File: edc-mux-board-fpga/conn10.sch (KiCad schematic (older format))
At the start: 24 parts

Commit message: Finished FPGA and MCU interconnections.
Finished up interrupt wiring
Fixed a few missing connections
Annotated Schematic
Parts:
- removed C? (x2): 1uF, Capacitor_SMD:C_0805_2012Metric, symbol Device:C_Small
- removed C? (x2): 2.2uF X7R, Capacitor_SMD:C_0603_1608Metric, symbol Device:C_Small
- removed C? (x2): 1uF, Capacitor_SMD:C_0603_1608Metric, symbol Device:C_Small
- removed C? (x8): 100nF, Capacitor_SMD:C_0603_1608Metric, symbol Device:C_Small
- removed C? (x2): 33pF, Capacitor_SMD:C_0603_1608Metric, symbol Device:C_Small
- removed C? (x2): 10uF, Capacitor_SMD:C_1206_3216Metric, symbol Device:C_Small
- removed FB?: 220Ω/2A, Resistor_SMD:R_0603_1608Metric, symbol Device:Ferrite_Bead_Small
- removed R? (x2): 750Ω, Resistor_SMD:R_0603_1608Metric, symbol Device:R_Small_US
- removed U?: TLV320AIC3206, Package_DFN_QFN:UQFN-40-1EP_5x5mm_P0.4mm_EP3.8x3.8mm_ThermalVias, symbol SW-Texas:TLV320AIC3206
- removed U?: MAX4910, Package_DFN_QFN:TQFN-16-1EP_3x3mm_P0.5mm_EP1.23x1.23mm, symbol SW-dallas-semi-maxim:MAX4910
- removed U?: P82B96, Package_SO:TSSOP-8_3x3mm_P0.65mm, symbol Interface_Expansion:P82B96
- added C185, C202: 2.2uF X7R, Capacitor_SMD:C_0603_1608Metric, symbol Device:C_Small
- added C186, C188, C189, C192, C193, C194, C195, C200: 100nF, Capacitor_SMD:C_0603_1608Metric, symbol Device:C_Small
- added C187, C197: 10uF, Capacitor_SMD:C_1206_3216Metric, symbol Device:C_Small
- added C190, C191: 33pF, Capacitor_SMD:C_0603_1608Metric, symbol Device:C_Small
- added C196, C201: 1uF, Capacitor_SMD:C_0603_1608Metric, symbol Device:C_Small
- added C198, C199: 1uF, Capacitor_SMD:C_0805_2012Metric, symbol Device:C_Small
- added FB13: 220Ω/2A, Resistor_SMD:R_0603_1608Metric, symbol Device:Ferrite_Bead_Small
- added R35, R36: 750Ω, Resistor_SMD:R_0603_1608Metric, symbol Device:R_Small_US
- added U34: MAX4910, Package_DFN_QFN:TQFN-16-1EP_3x3mm_P0.5mm_EP1.23x1.23mm, symbol SW-dallas-semi-maxim:MAX4910
- added U35: TLV320AIC3206, Package_DFN_QFN:UQFN-40-1EP_5x5mm_P0.4mm_EP3.8x3.8mm_ThermalVias, symbol SW-Texas:TLV320AIC3206
- added U36: P82B96, Package_SO:TSSOP-8_3x3mm_P0.65mm, symbol Interface_Expansion:P82B96
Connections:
- net +12V: now also C200.1, R35.1, R36.1, U36.8 (VCC)
- net +1V8: now also C188.2, C192.2, U35.30 (VSYS), U35.40 (DVDD)
- net +1V8A: now also C195.2, C196.2, C197.2, U35.29 (AVDD), U35.32 (DRVDD_HP), U35.39 (DVDD_CP)
- net +3V3: now also C186.2, C187.1, C189.2, U34.14 (VCC), U35.10 (IOVDD)
- net AUD_GND: now also U34.4 (COM2)
- net BCLK: now also U35.6 (BCLK)
- net DIN: now also U35.8 (DIN)
- net DOUT: now also U35.9 (DOUT)
- net GND: now also C186.1, C187.2, C188.1, C189.1, C190.1, C191.1, C192.1, C193.1, C194.1, C195.1, C196.1, C197.1, C200.2, C201.1, C202.1, FB13.2, U34.17 (PAD), U34.5 (NC2), U34.6 (GND), U35.1 (DVSS), U35.11 (IOVSS), U35.16 (SPI_SELECT), U35.2 (DVSS), U35.21 (AVSS), U35.37 (DVSS_CP), U35.41 (PAD), U36.4 (GND)
- net HP_~LINE~_SEL: now also U34.10 (CB2), U34.2 (CB1), U35.4 (INT2_OUT)
- net L_IN: now also C190.2, U35.17 (IN1_L)
- net L_OUT: now also U34.16 (COM1)
- net MCLK: now also U35.5 (MCLK)
- net R_IN: now also C191.2, U35.18 (IN1_R)
- net R_OUT: now also U34.8 (COM3)
- net SCL: now also U35.13 (SCL), U36.7 (SCL)
- net SCL_HV: now also R36.2, U36.5 (TXD-SCL), U36.6 (RXD-SCL)
- net SDA: now also U35.14 (SDA), U36.1 (SDA)
- net SDA_HV: now also R35.2, U36.2 (RXD-SDA), U36.3 (TXD-SDA)
- net WCLK: now also U35.7 (WCLK)
- net ~RESET: now also U35.3 (~RESET)
- new net: C198.1, U34.1 (NC1)
- new net: C198.2, U35.26 (LINE_OUT_L)
- new net: C199.1, U34.9 (NC3)
- new net: C199.2, U35.27 (LINE_OUT_R)
- new net: C193.2, U35.19 (IN2_L), U35.20 (IN2_R)
- new net: C201.2, U35.22 (REF)
- new net: C194.2, U35.24 (IN3_L), U35.25 (IN3_R)
- new net: FB13.1, U34.3 (NO2), U35.28 (GND_SENSE)
- new net: U34.15 (NO1), U35.31 (HPL)
- new net: U34.7 (NO3), U35.33 (HPR)
- new net: C202.2, U35.35 (VNEG)
- new net: C185.1, U35.36 (FLY_N)
- new net: C185.2, U35.38 (FLY_P)

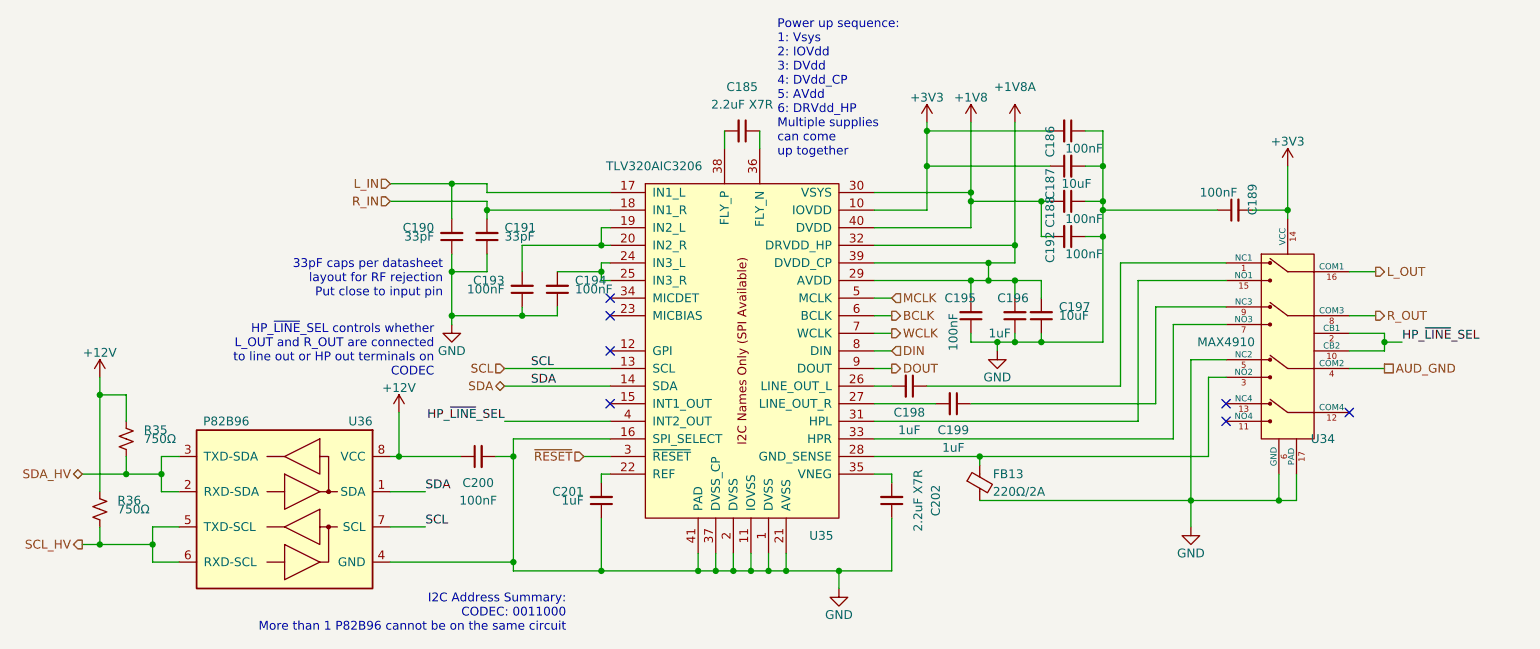
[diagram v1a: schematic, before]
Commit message: assigned more footprints
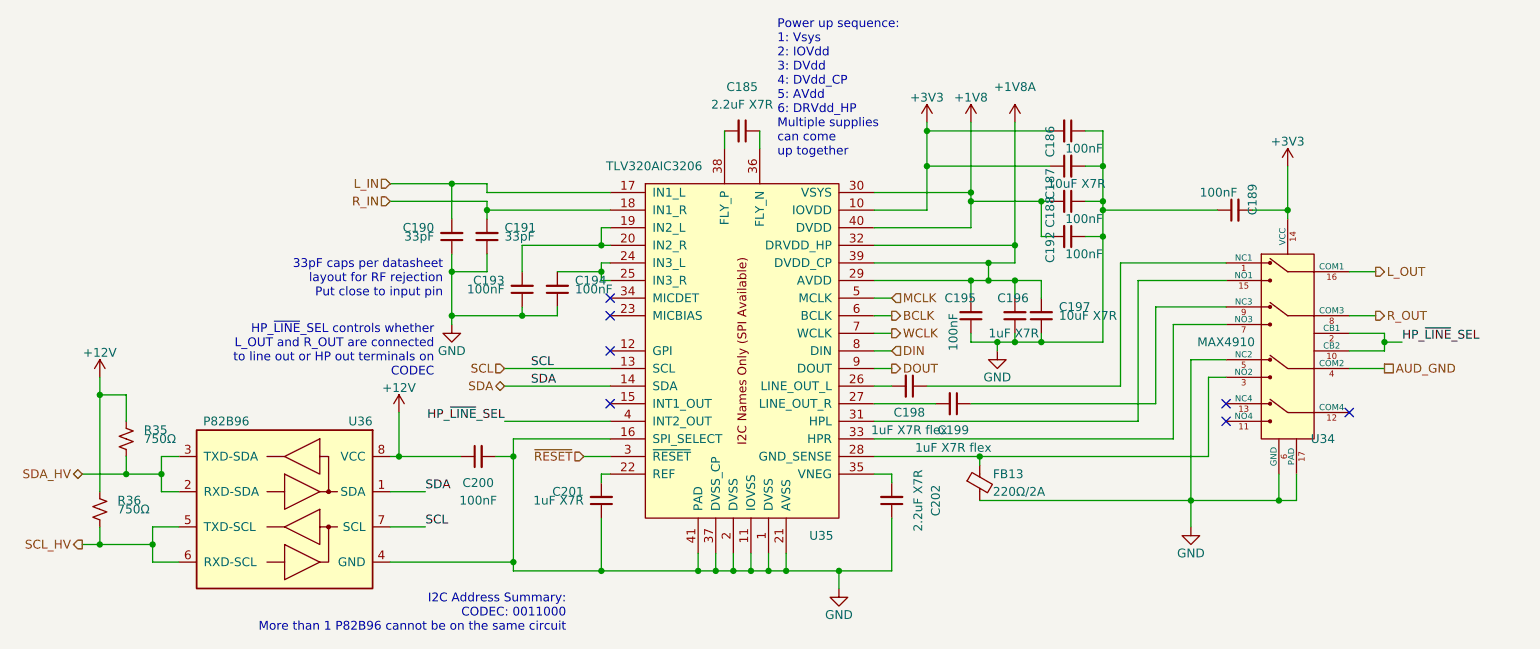
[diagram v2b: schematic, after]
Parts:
- C187, C197: value 10uF -> 10uF X7R
- C196, C201: value 1uF -> 1uF X7R
- C198, C199: value 1uF -> 1uF X7R flex
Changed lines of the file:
@@
 P 4400 4250
 F 0 "C201" H 4500 4200 50  0000 L CNN
-F 1 "1uF" H 4500 4250 50  0000 L CNN
+F 1 "1uF X7R" H 4500 4250 50  0000 L CNN
 F 2 "Capacitor_SMD:C_0603_1608Metric" H 4400 4250 50  0001 C CNN
 F 3 "~" H 4400 4250 50  0001 C CNN
@@
 P 6750 3200
 F 0 "C196" H 6850 3100 50  0000 R CNN
-F 1 "1uF" H 6900 3300 50  0000 R CNN
+F 1 "1uF X7R" H 6900 3300 50  0000 R CNN
 F 2 "Capacitor_SMD:C_0603_1608Metric" H 6750 3200 50  0001 C CNN
 F 3 "~" H 6750 3200 50  0001 C CNN
@@
 P 6900 3200
 F 0 "C197" H 6800 3150 50  0000 R CNN
-F 1 "10uF" H 6800 3200 50  0000 R CNN
+F 1 "10uF X7R" H 6800 3200 50  0000 R CNN
 F 2 "Capacitor_SMD:C_1206_3216Metric" H 6900 3200 50  0001 C CNN
 F 3 "~" H 6900 3200 50  0001 C CNN
@@
 P 7050 2350
 F 0 "C187" H 6950 2450 50  0000 C CNN
-F 1 "10uF" V 6950 2300 50  0000 C CNN
+F 1 "10uF X7R" V 6950 2300 50  0000 C CNN
 F 2 "Capacitor_SMD:C_1206_3216Metric" H 7050 2350 50  0001 C CNN
 F 3 "~" H 7050 2350 50  0001 C CNN
@@
 P 6150 3600
 F 0 "C198" V 6300 3600 50  0000 C CNN
-F 1 "1uF" V 6400 3600 50  0000 C CNN
+F 1 "1uF X7R flex" V 6400 3600 50  0000 C CNN
 F 2 "Capacitor_SMD:C_0805_2012Metric" H 6150 3600 50  0001 C CNN
 F 3 "~" H 6150 3600 50  0001 C CNN
@@
 P 6400 3700
 F 0 "C199" V 6550 3700 50  0000 C CNN
-F 1 "1uF" V 6650 3700 50  0000 C CNN
+F 1 "1uF X7R flex" V 6650 3700 50  0000 C CNN
 F 2 "Capacitor_SMD:C_0805_2012Metric" H 6400 3700 50  0001 C CNN
 F 3 "~" H 6400 3700 50  0001 C CNN

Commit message: re-annotating after adding power ICs and decoupling capacitors.
Also verified most footprints, and updated schematic field data.
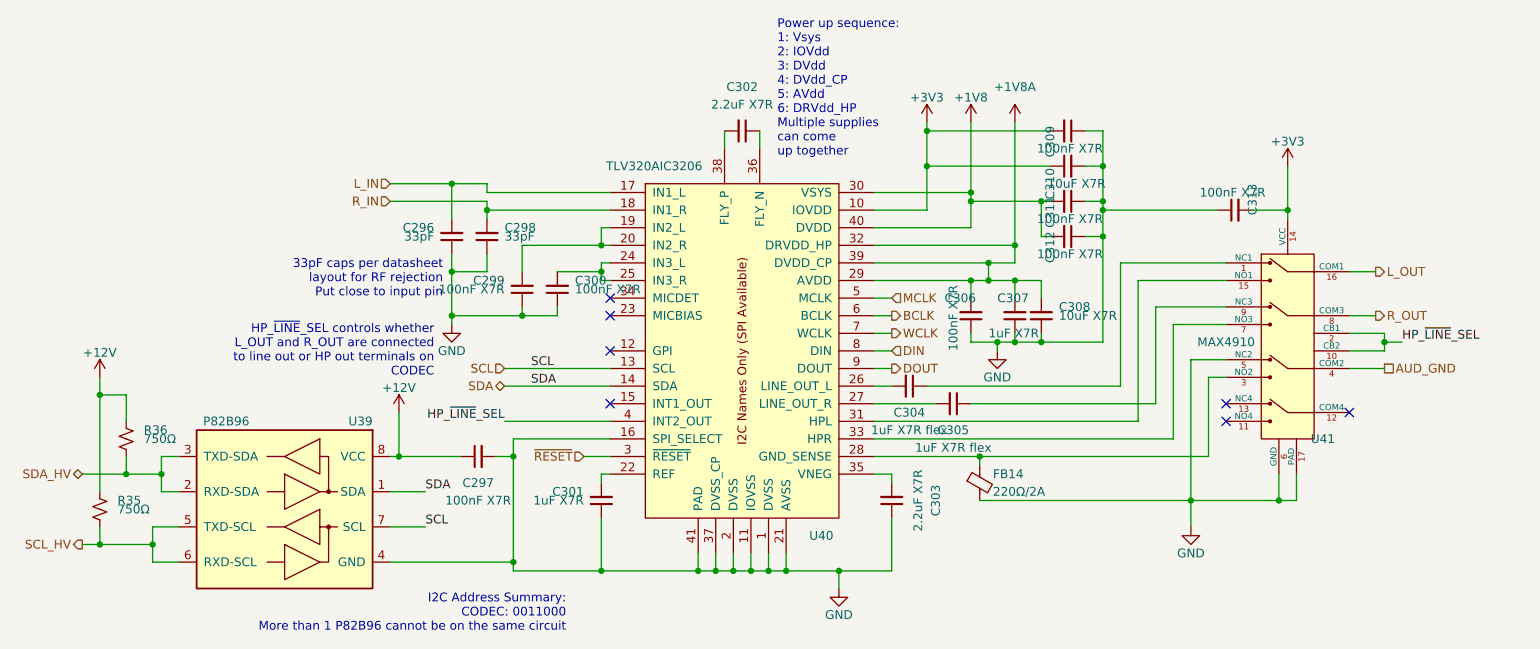
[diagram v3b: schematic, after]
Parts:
- C297: renamed from C200; value 100nF -> 100nF X7R
- C299: renamed from C193; value 100nF -> 100nF X7R
- C300: renamed from C194; value 100nF -> 100nF X7R
- C306: renamed from C195; value 100nF -> 100nF X7R
- C309: renamed from C186; value 100nF -> 100nF X7R
- C311: renamed from C188; value 100nF -> 100nF X7R
- C312: renamed from C192; value 100nF -> 100nF X7R
- C313: renamed from C189; value 100nF -> 100nF X7R
- R35: renamed from R36; Package ID (none) -> 0402in/1005mm
- R36: renamed from R35; Package ID (none) -> 0402in/1005mm
- renumbered C190 to C296, C191 to C298, C201 to C301, C185 to C302, C202 to C303, C198 to C304, C199 to C305, C196 to C307, C197 to C308, C187 to C310, FB13 to FB14, U36 to U39, U35 to U40, U34 to U41

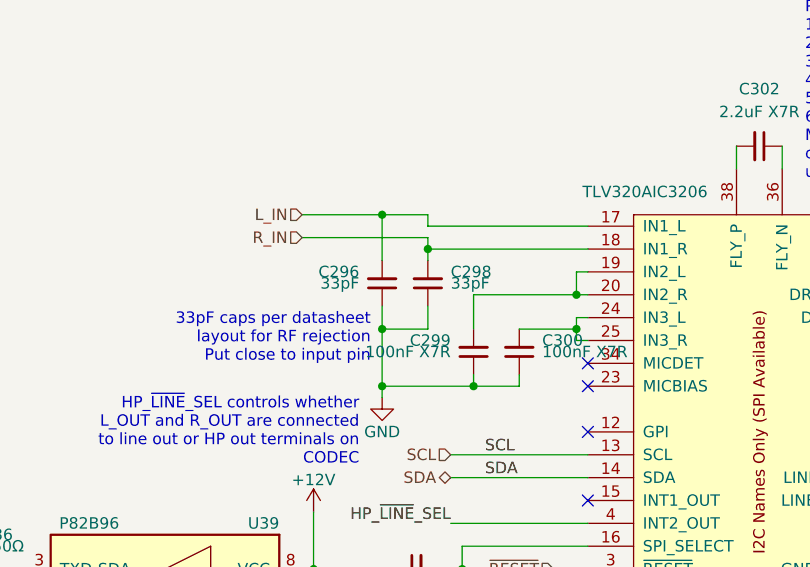
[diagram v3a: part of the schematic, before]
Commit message: Reannotating and adding more fields to components
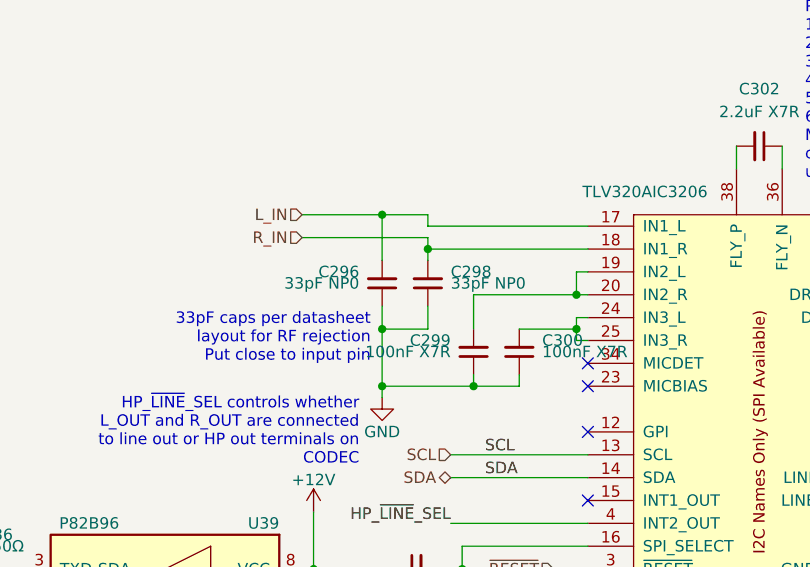
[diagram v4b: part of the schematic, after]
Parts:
- C296, C298: value 33pF -> 33pF NP0; footprint Capacitor_SMD:C_0603_1608Metric -> Capacitor_SMD:C_0402_1005Metric; Characteristics (none) -> CAP CER 33PF 25V NP0 0402; Description (none) -> MLCC Capacitor; Manufacturer (none) -> AVX; Manufacturers Part Number (none) -> 04023A330FAT2A; Package ID 0603in/1608mm -> 0402in/1005mm
- C297, C299, C300, C306, C309, C311, C312, C313: Characteristics (none) -> CAP CER 0.1UF 25V X7R 0603; Description (none) -> MLCC Capacitor; Manufacturer (none) -> Kemet; Manufacturers Part Number (none) -> C0603C104J3RACAUTO
- C301, C307: Characteristics (none) -> CAP CER 1UF 25V X7R 0603; Description (none) -> MLCC Capacitor
- C302, C303: footprint Capacitor_SMD:C_0603_1608Metric -> Capacitor_SMD:C_0805_2012Metric; Characteristics (none) -> CAP CER 2.2UF 25V X7R 0805; Description (none) -> MLCC Capacitor; Manufacturer (none) -> TDK; Manufacturers Part Number (none) -> CGA4J3X7R1E225K125AB; Package ID 0603in/1608mm -> 0805in/2012mm
- C304, C305: Characteristics (none) -> CAP CER 0805 1UF 25V X7R 5%; Description (none) -> MLCC Capacitor; Manufacturers Part Number C0805X105J3RACAUTO -> C0805X105J3RECAUTO
- C308, C310: Characteristics (none) -> CAP CER 10UF 25V X7R 1206; Description (none) -> MLCC Capacitor
- FB14: footprint Resistor_SMD:R_0603_1608Metric -> Inductor_SMD:L_0603_1608Metric; Description (none) -> Ferrite Bead
- R35, R36: Description (none) -> Resistor
- U39: Description (none) -> I2C Buffer / Voltage Translator; Manufacturer (none) -> Texas Instruments; Manufacturers Part Number (none) -> P82B96; Package ID (none) -> TSSOP8
- U40: Description (none) -> I2S Audio Codec; Manufacturer (none) -> Texas Instruments; Package ID (none) -> UQFN40
- U41: Description (none) -> Clickless Audio Switch; Manufacturer (none) -> Maxim Integrated; Package ID (none) -> TQFN16

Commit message: Fixed resistor footprint
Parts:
- R35, R36: footprint Resistor_SMD:R_0603_1608Metric -> Resistor_SMD:R_0402_1005Metric
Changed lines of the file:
@@
 F 0 "R36" H 1800 3950 50  0000 L CNN
 F 1 "750Ω" H 1800 3900 50  0000 L CNN
-F 2 "Resistor_SMD:R_0603_1608Metric" H 1700 3900 50  0001 C CNN
+F 2 "Resistor_SMD:R_0402_1005Metric" H 1700 3900 50  0001 C CNN
 F 3 "~" H 1700 3900 50  0001 C CNN
 F 4 "0402in/1005mm" H 0   0   50  0001 C CNN "Package ID"
@@
 F 0 "R35" H 1650 4350 50  0000 L CNN
 F 1 "750Ω" H 1650 4300 50  0000 L CNN
-F 2 "Resistor_SMD:R_0603_1608Metric" H 1550 4300 50  0001 C CNN
+F 2 "Resistor_SMD:R_0402_1005Metric" H 1550 4300 50  0001 C CNN
 F 3 "~" H 1550 4300 50  0001 C CNN
 F 4 "0402in/1005mm" H 0   0   50  0001 C CNN "Package ID"
